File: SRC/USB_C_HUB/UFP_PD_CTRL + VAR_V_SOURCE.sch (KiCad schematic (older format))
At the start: 46 parts

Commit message: ALL DONE BUT THE HDMI SECTION. NEED FOOTPRINT ASSIGNMENT
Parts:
- removed C? (x3): 10uF, symbol Device:C_Small
- removed C? (x2): 47uF, symbol Device:C_Small
- removed C?: 1uF, symbol Device:C_Small
- removed C?: 0.01uF, symbol Device:C_Small
- removed C? (x2): 220pF, symbol Device:C_Small
- removed D?: D_Schottky, symbol Device:D_Schottky
- removed L?: 10uH, symbol OLIMEX_RCL:INDUCTOR_SMALL
- removed R?: 10K_603, symbol Device:R_US
- removed R?: 30K_603, symbol Device:R_US
- removed R?: 20K_603, symbol Device:R_US
- removed R?: 5K_805, symbol Device:R_US
- removed R?: 100K, symbol Device:R_US
- removed R? (x2): 0, symbol Device:R_US
- removed U?: TPS65987D, symbol usb_hub:TPS65987D
- added C24, C26, C27: 1uF, symbol Device:C_Small
- added C29: 0.1uF, symbol Device:C_Small
- added C30, C31: 4.7uF, symbol Device:CP_Small
- added IC1: STUSB4700YQTR, SamacSys_Parts_2:QFN50P400X400X100-25N, symbol SamacSys_Parts:STUSB4700YQTR
- added L1: SRP1038A-100M, SamacSys_Parts_2:INDPM110100X400N, symbol SamacSys_Parts:SRP1038A-100M
- added Q2: BSH105,215, Package_TO_SOT_SMD:SC-59, symbol dk_Transistors-FETs-MOSFETs-Single:2N7002P_215
- added Q3: RQ5E025ATTCL, SamacSys_Parts_2:SOT95P280X100-3N, symbol SamacSys_Parts:RQ5E025ATTCL
- added R11, R12, R13, R21: 100K, symbol Device:R_US
- added R19, R26: 10K, symbol Device:R_US
- added R20: 2.2K, symbol Device:R_US
- added R22: 3K_603, symbol Device:R_US
- added R23: 2.4K_603, symbol Device:R_US
- added R24: 820, symbol Device:R_US
- added U8: SQJ951EP, SamacSys_Parts_2:SQJ968EPT1GE3, symbol usb_hub:SQJ951EP
- gave numbers to parts that had none: 27
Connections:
- net +3V3: now also IC1.17 (A_B_SIDE)
- net GND: now also C25.2, R15.2, R16.2, R18.2, R25.2, R27.2, R28.2, R29.2, C24.1, C26.2, C27.2, IC1.1 (NC_1_GND), IC1.10 (GND), IC1.22 (VSYS), IC1.25 (EP), IC1.3 (VCONN), IC1.5 (NC_2_GND), IC1.6 (RESET), R11.2, R12.2, R13.2, R21.2, R23.2, R24.2
- net VBUS: now also IC1.18 (VBUS_SENSE), U8.5 (D)
- net at D10.K, R14.1, U7.6 (D)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: now also L1.1
- net at C25.1, C28.2, Q1.3 (D)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: now also Q2.3 (D)
- net POWER_PATH: now reaches C28.1, R17.1
- net POWER_PATH: now also C24.2, C29.1, C30.1, C31.1, IC1.24 (VDD), L1.2, Q3.2, R26.1, U8.6 (D)
- net POWER_LVL1 renamed PWR_LVL1_9V
- net PWR_LVL1_9V: now also IC1.12 (GPIO0)
- net POWER_LVL2 renamed PWR_LVL2_15V
- net PWR_LVL2_15V: now also IC1.14 (GPIO2)
- net POWER_LVL3 renamed PWR_LVL3_20V
- net PWR_LVL3_20V: now also IC1.15 (GPIO3)
- net SYS_PWR renamed PWR_FRM_SNK
- new net: C26.1, IC1.23 (VREG_2V7)
- new net: C27.1, IC1.21 (VREG_1V2)
- new net: IC1.13 (VVAR_ADDR0), R12.1
- new net: C29.2, C30.2, C31.2
- new net: R19.1, U8.1 (S), U8.3 (S)
- new net: R19.2, R20.1, U8.2 (G), U8.4 (G)
- new net: IC1.20 (VBUS_EN_SRC), R20.2
- new net: Q3.3, R24.1
- new net: IC1.7 (SCL), R13.1
- new net: IC1.8 (SDA), R11.1
- new net: R22.2, R23.1
- new net: Q2.2 (S), R22.1
- new net CC1: IC1.2 (CC1)
- new net CC2: IC1.4 (CC2)
- new net PWR_LVL_12V: IC1.11 (GPIO1), Q2.1 (G), R21.1
- new net VBUS_DISCH: IC1.19 (VBUS_DISCH), Q3.1, R26.2
- no-connect marks 0 -> 2
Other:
- note added: "NEED TOTAL \n5.42K\nR1=3K + R2=2.4K\n"
- note added: "OPEN DRAIN INPUT\nIf theres a flip, then it\n turn on meaning the \noutput signal will go low. \nNO FLIP= output==HIGH"
- note added: "POWER PATH FLOW"
- note removed: "BP_WaitFor3V3_Internal mode\ndiv=0.25, SPI_POCI=1\nR1=30K, R2=10K."
- note removed: "The TPS65987D requires firmware \nprogramming via a downloadable GUI tool.\nRecomendation: Since the system takes in a \ncharger we can configure it as a Source device\n(read:https://www.embedded.com/usb-type-c-and-power-delivery-101-ports-and-connections/) \nSecondly: we can configure it as a DRP device that can source(provide) or sink(receive) power. Its a source when the charging \nreceptacle 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"
- note removed: "sets the I2C address\nDIV = R2/(R1+R2)\nR1=5K, R2=20K\nDIV=0.8, ADD=011b"
- moved on the sheet: C20, C21, C22, C23, C25, C28, D10, D7, D8, D9, Q1, Q4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

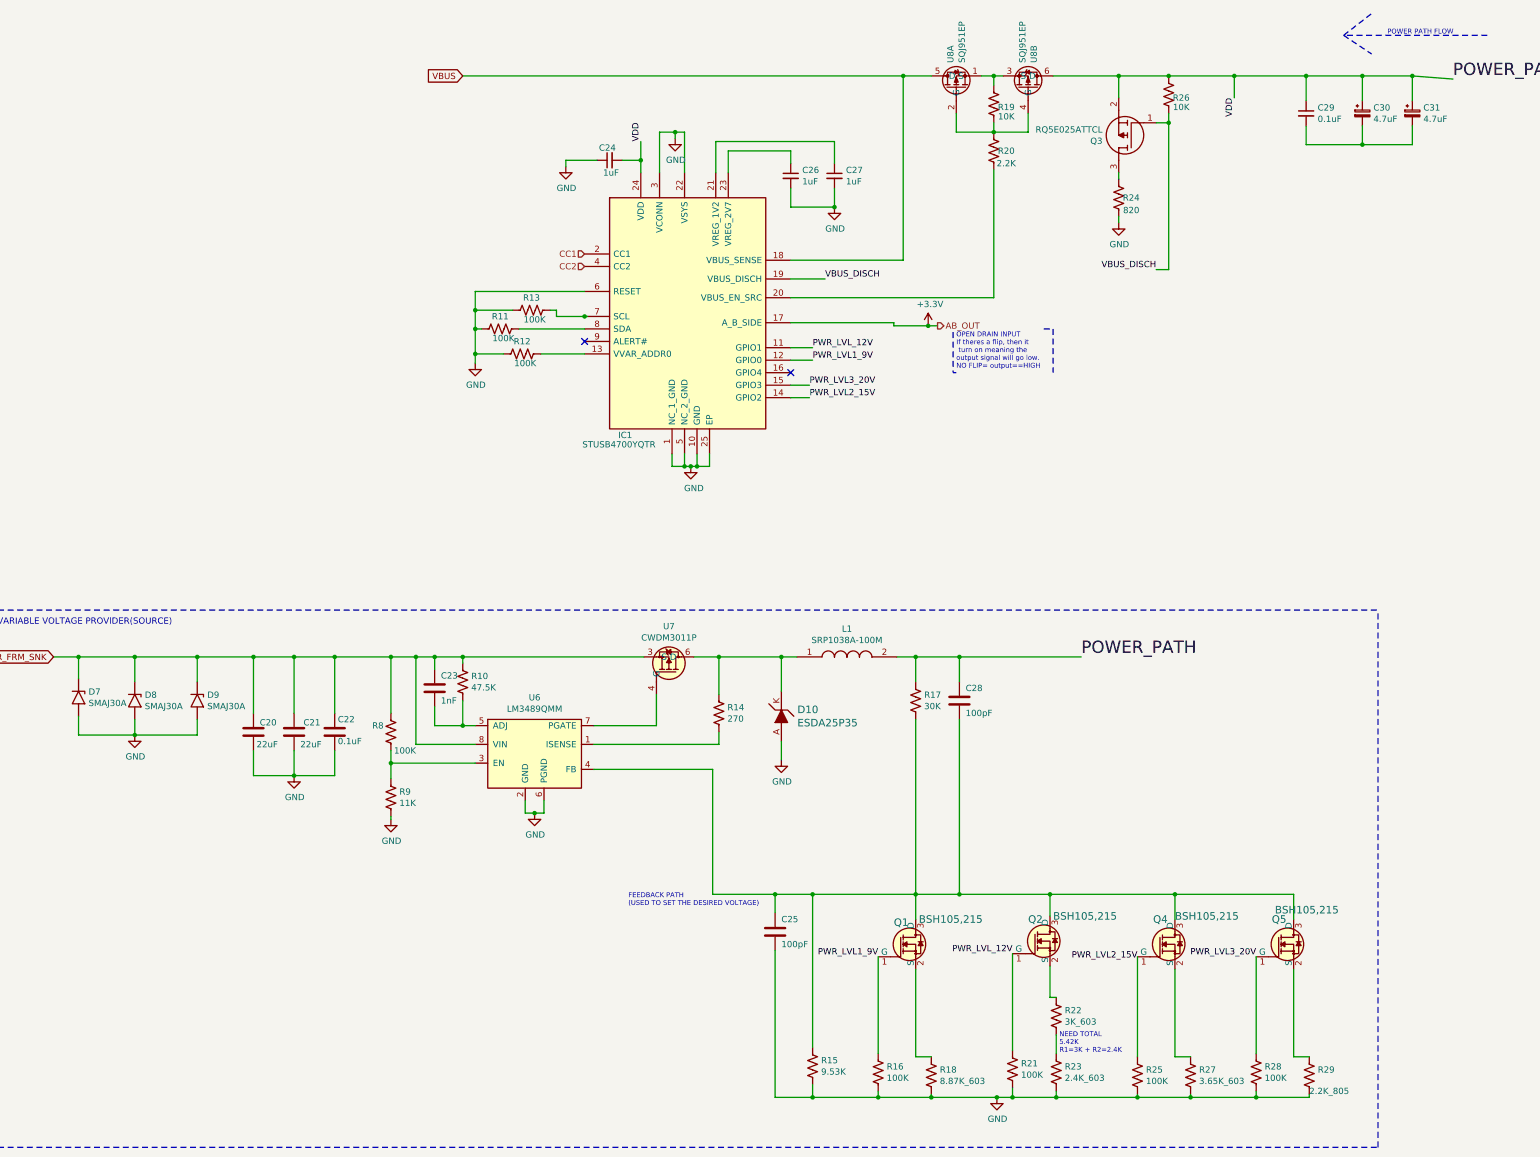
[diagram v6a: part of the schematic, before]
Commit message: schematic capture complete. Pending Footprint assignment. accetable Errors=21
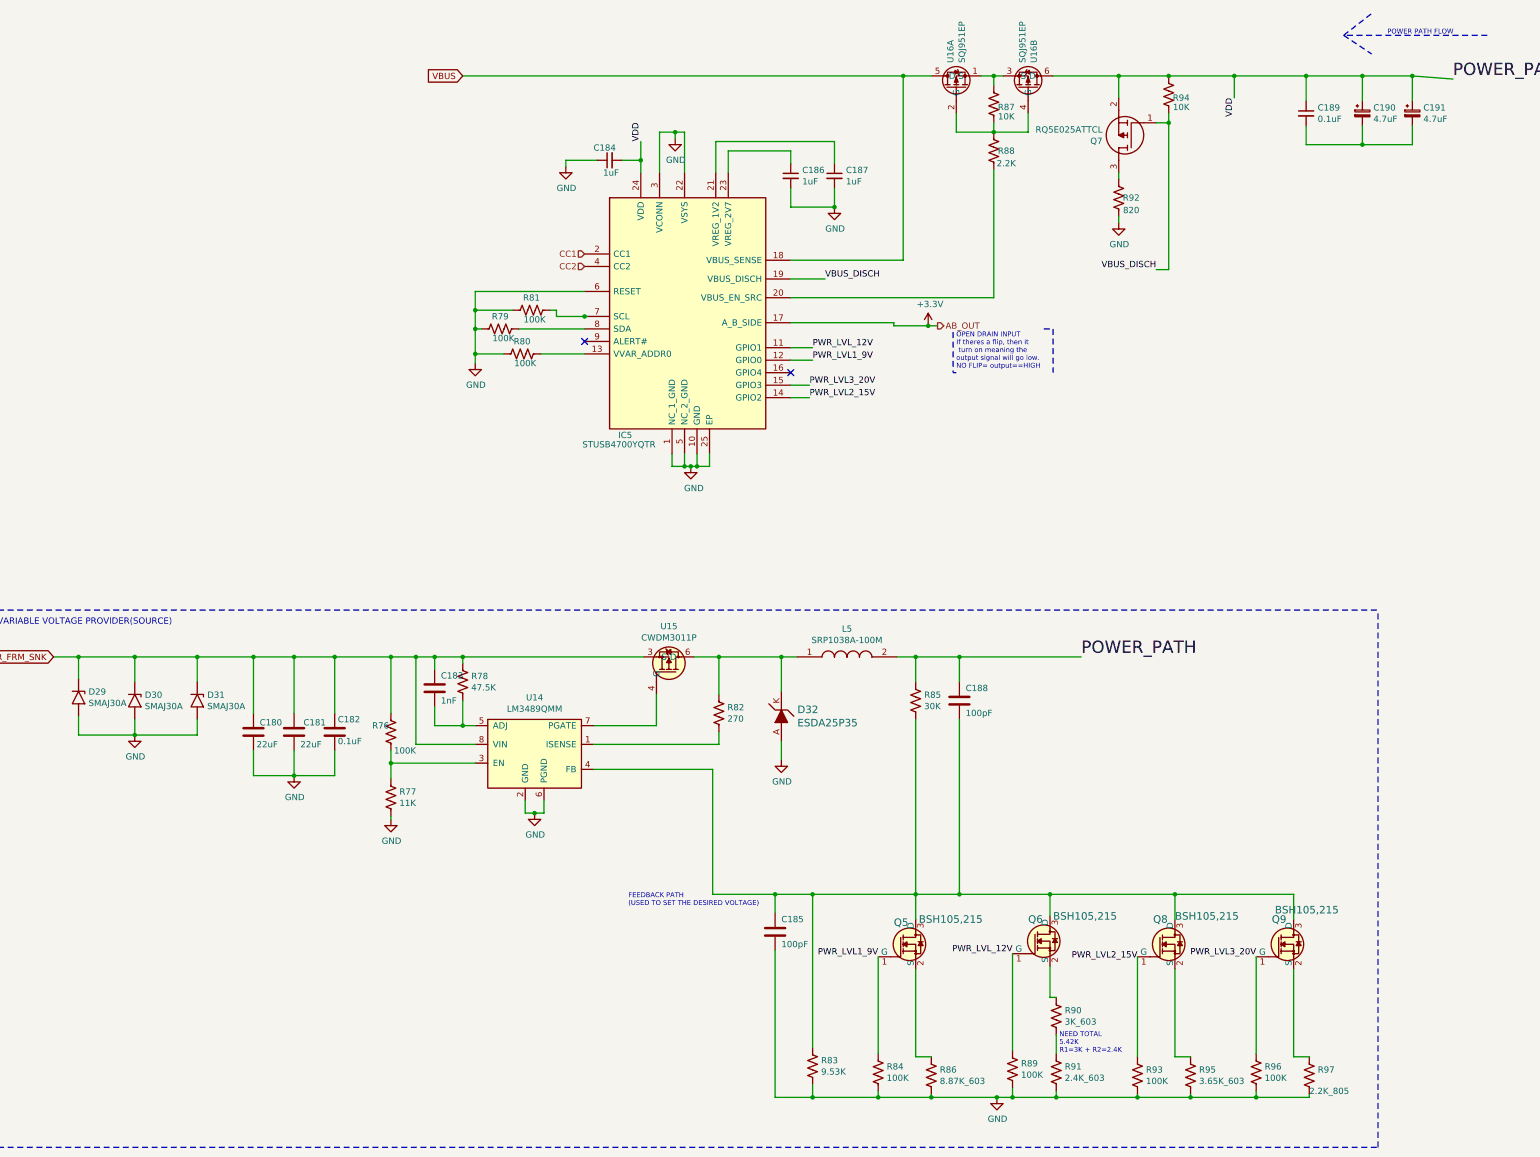
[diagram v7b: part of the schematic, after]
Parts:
- renumbered C20 to C180, C21 to C181, C22 to C182, C23 to C183, C24 to C184, C25 to C185, C26 to C186, C27 to C187, C28 to C188, C29 to C189, C30 to C190, C31 to C191, D7 to D29, D8 to D30, D9 to D31, D10 to D32, IC1 to IC5, L1 to L5, Q1 to Q5, Q2 to Q6, Q3 to Q7, Q4 to Q8, Q5 to Q9, R8 to R76, R9 to R77, R10 to R78, R11 to R79, R12 to R80, R13 to R81, R14 to R82, R15 to R83, R16 to R84, R17 to R85, R18 to R86, R19 to R87, R20 to R88, R21 to R89, R22 to R90, R23 to R91, R24 to R92, R25 to R93, R26 to R94, R27 to R95, R28 to R96, R29 to R97, U6 to U14, U7 to U15, U8 to U16
